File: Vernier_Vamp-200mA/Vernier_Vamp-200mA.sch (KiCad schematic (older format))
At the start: 6 parts, among them J1 Conn_01x02, J2 RJ45, J3 Screw_Terminal_01x04, J5 Conn_Coaxial, J6 Conn_Coaxial, J7 Conn_Coaxial

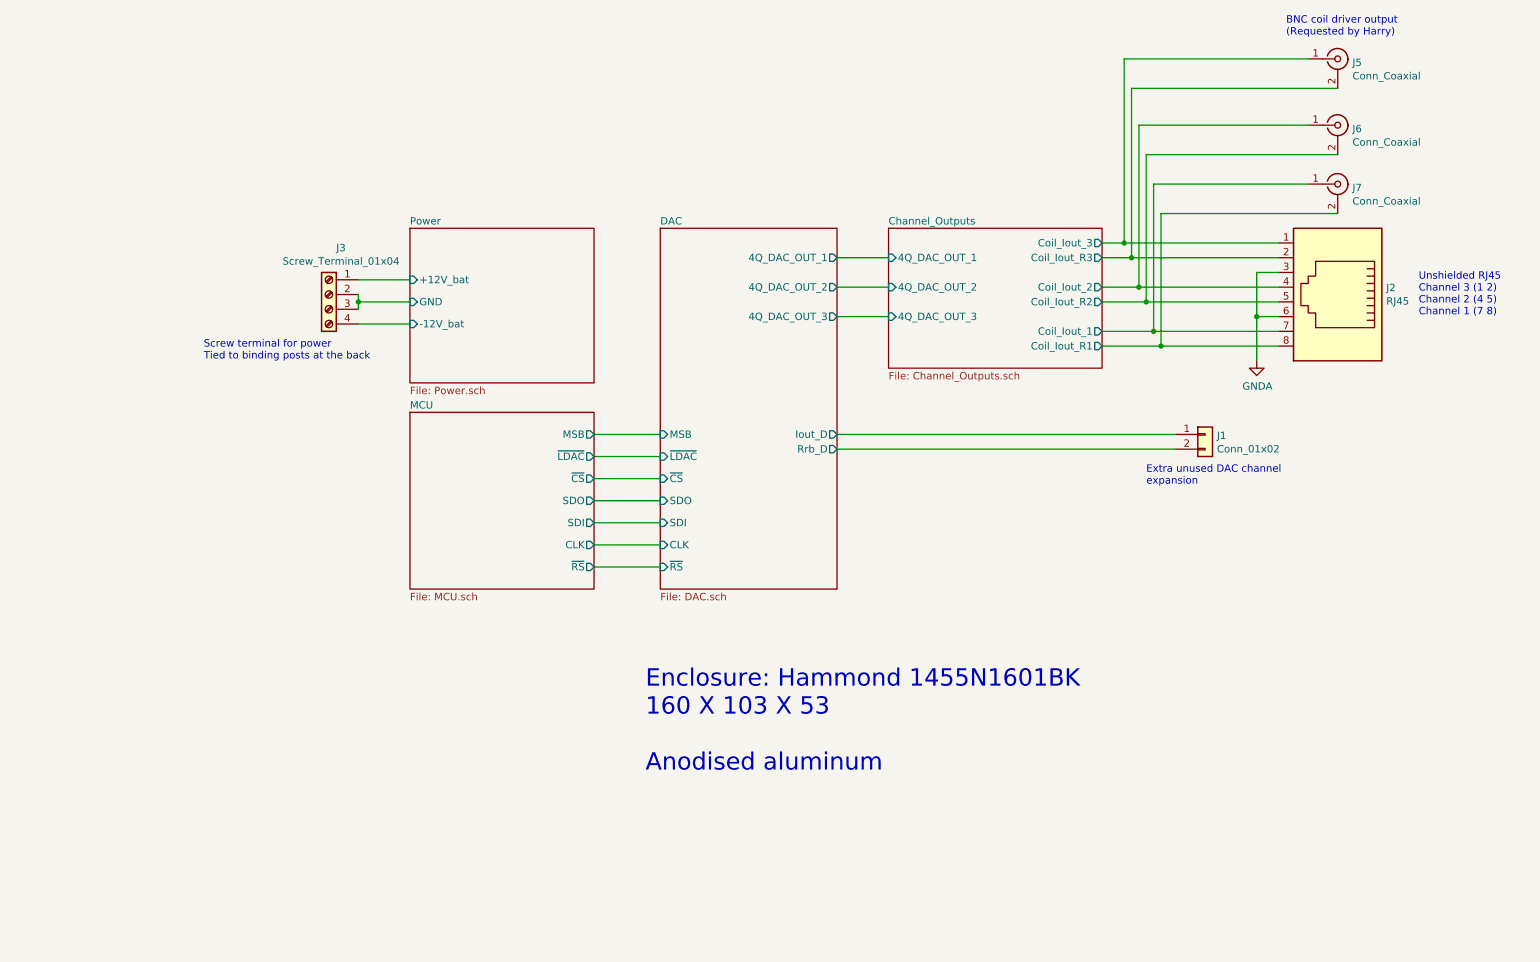
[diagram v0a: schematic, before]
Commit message: Coil driver version 1.0B
Updated coil driver 200mA version with fixes requested by Iain.
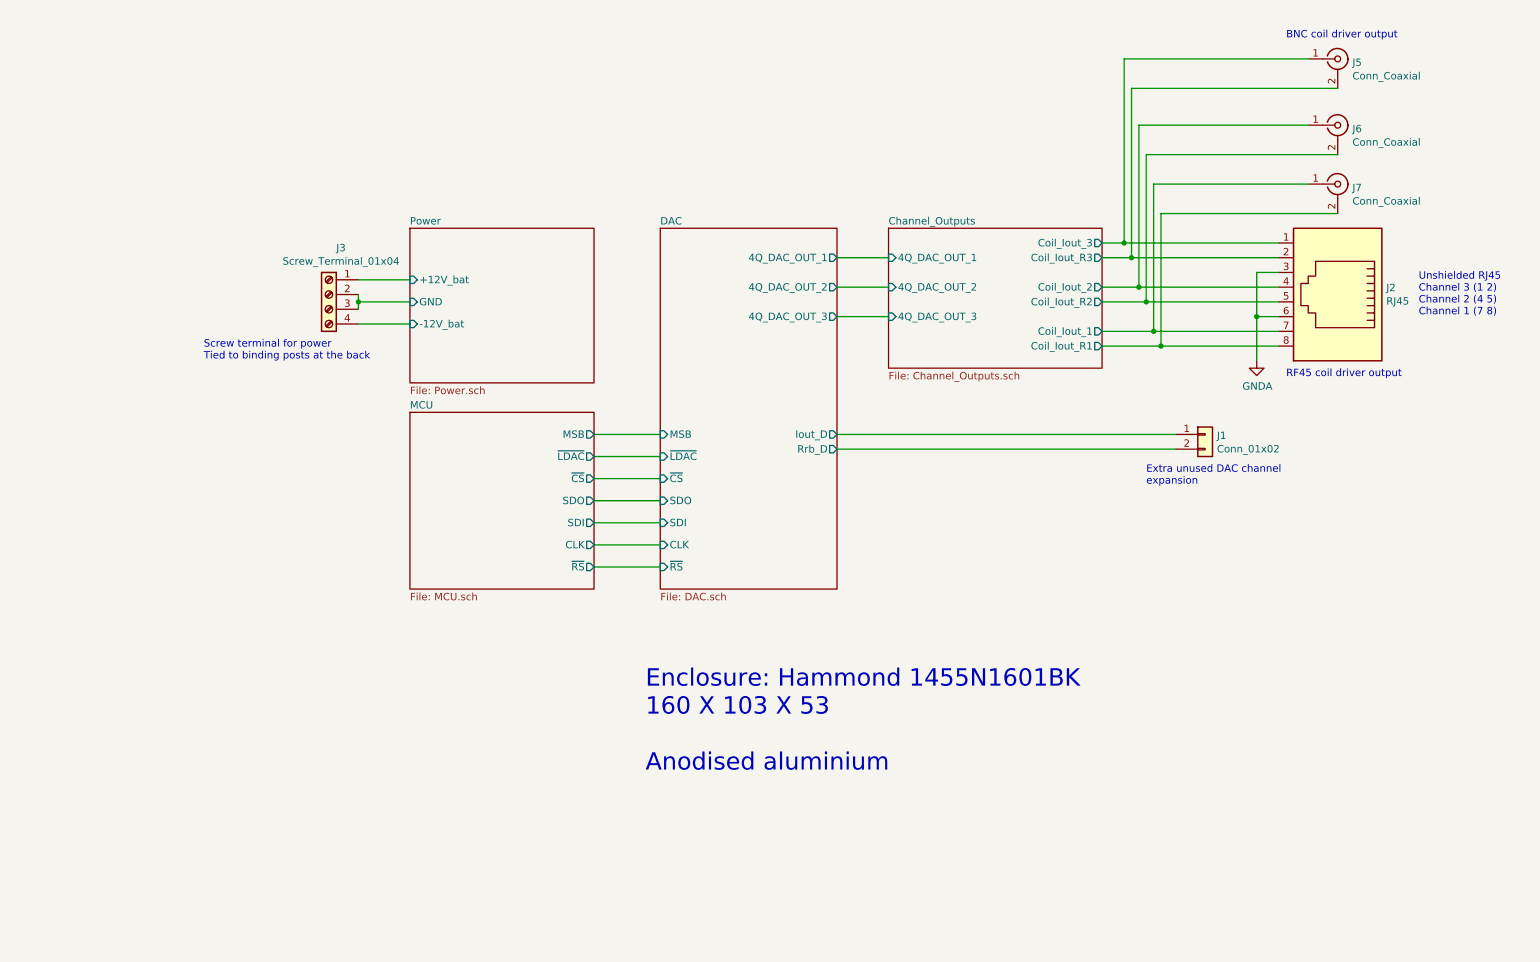
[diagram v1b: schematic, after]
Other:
- note added: "BNC coil driver output\n\n"
- note added: "Enclosure: Hammond 1455N1601BK\n160 X 103 X 53\n\nAnodised aluminium"
- note added: "RF45 coil driver output\n\n"
- note removed: "BNC coil driver output\n(Requested by Harry)"
- note removed: "Enclosure: Hammond 1455N1601BK\n160 X 103 X 53\n\nAnodised aluminum"
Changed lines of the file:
@@
 $Descr A4 11693 8268
 encoding utf-8
-Sheet 1 5
+Sheet 1 7
 Title "\"Vernier Vamp\" Coil Driver - 200mA"
-Date "2020-02-04"
-Rev "1.0A"
+Date "2020-04-27"
+Rev "1.0B"
 Comp "Strathclyde University"
 Comment1 "Designed by: Marcin Mrozowski"
@@
 Wire Wire Line
 	8400 3600 8000 3600
-Text Notes 9250 1500 0    50   ~ 0
-BNC coil driver output\n(Requested by Harry)
+Text Notes 9250 1600 0    50   ~ 0
+BNC coil driver output\n\n
 Text Notes 10150 3400 0    50   ~ 0
 Unshielded RJ45\nChannel 3 (1 2)\nChannel 2 (4 5)\nChannel 1 (7 8)
@@
 Screw terminal for power\nTied to binding posts at the back
 Text Notes 4900 6500 0    118  ~ 0
-Enclosure: Hammond 1455N1601BK\n160 X 103 X 53\n\nAnodised aluminum
+Enclosure: Hammond 1455N1601BK\n160 X 103 X 53\n\nAnodised aluminium
+Text Notes 9250 3900 0    50   ~ 0
+RF45 coil driver output\n\n
 $EndSCHEMATC

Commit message: Schematic and layout changes
Schematic updates:
- Added extra comments
- Added description (BNC channels)
- Moved mounting holes to the title block
- Added an option for connecting low battery indicatior LEDs to either +12V or GND (Comparator pulls to -12V)
- Added a 0R resistor for connecting +12V to Vin of nano
Layout:
- Added board ID and datecode on both sides
- Fixed priority of GND copper islands that were causing issues
- Changed the ground plane to be solid on the connection point (still not ideal but better)
- All components with thermal vias require tented vias so left as default
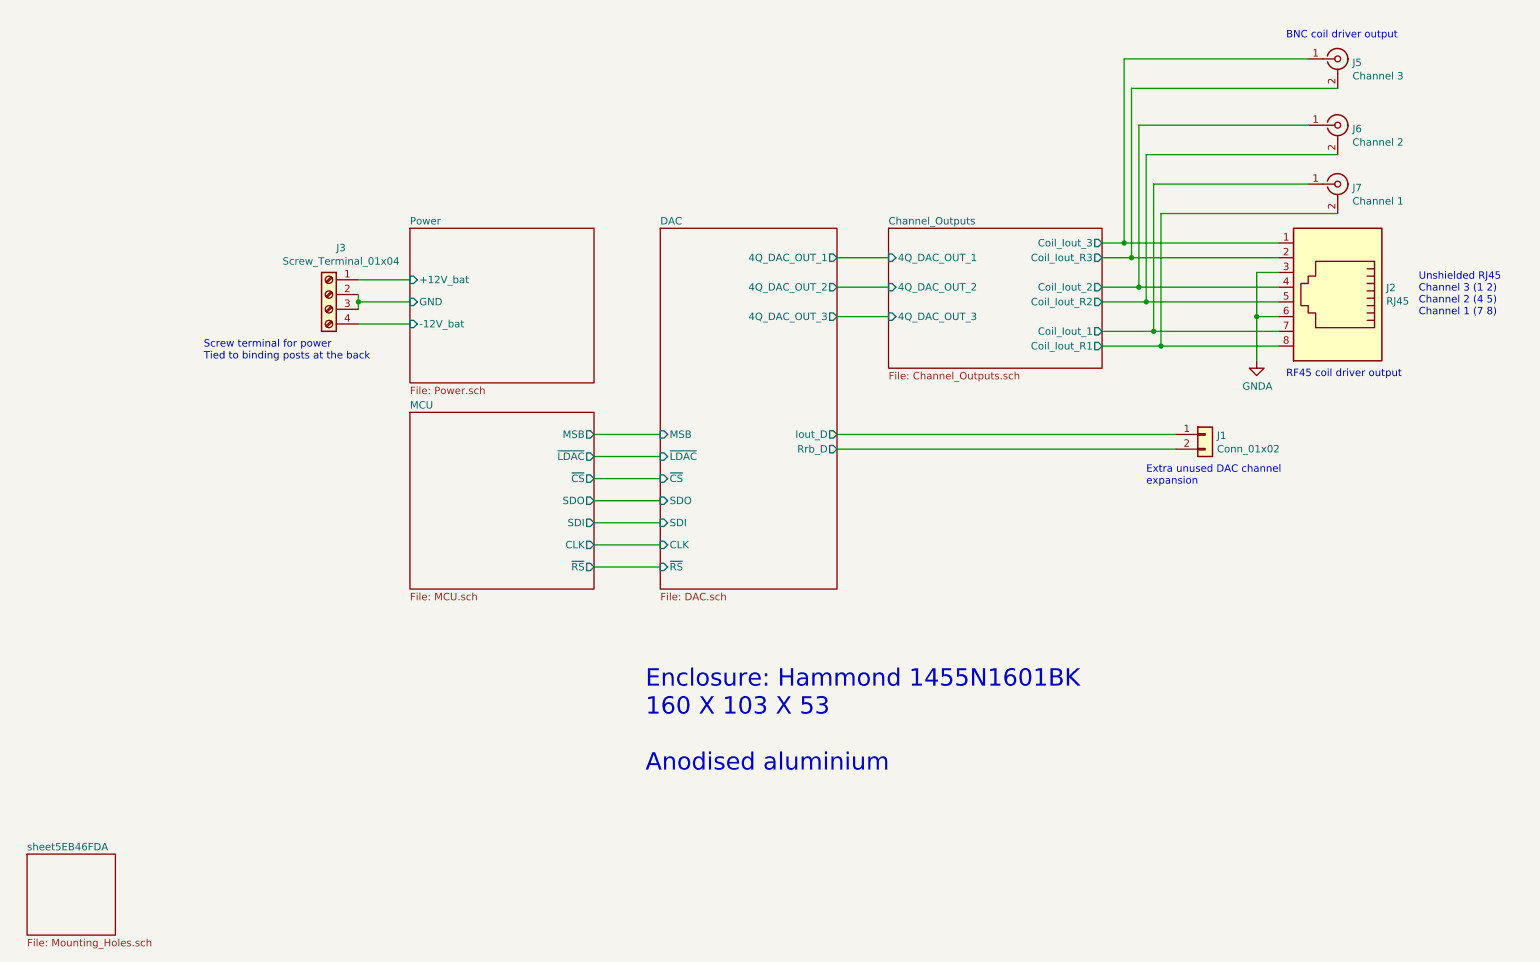
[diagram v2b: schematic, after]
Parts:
- J5: value Conn_Coaxial -> Channel 3
- J6: value Conn_Coaxial -> Channel 2
- J7: value Conn_Coaxial -> Channel 1
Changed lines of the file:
@@
 P 9600 1650
 F 0 "J5" H 9700 1625 50  0000 L CNN
-F 1 "Conn_Coaxial" H 9700 1534 50  0000 L CNN
+F 1 "Channel 3" H 9700 1534 50  0000 L CNN
 F 2 "Connector_Coaxial:BNC_Amphenol_031-6575_Horizontal" H 9600 1650 50  0001 C CNN
 F 3 " ~" H 9600 1650 50  0001 C CNN
@@
 P 9600 2100
 F 0 "J6" H 9700 2075 50  0000 L CNN
-F 1 "Conn_Coaxial" H 9700 1984 50  0000 L CNN
+F 1 "Channel 2" H 9700 1984 50  0000 L CNN
 F 2 "Connector_Coaxial:BNC_Amphenol_031-6575_Horizontal" H 9600 2100 50  0001 C CNN
 F 3 " ~" H 9600 2100 50  0001 C CNN
@@
 P 9600 2500
 F 0 "J7" H 9700 2475 50  0000 L CNN
-F 1 "Conn_Coaxial" H 9700 2384 50  0000 L CNN
+F 1 "Channel 1" H 9700 2384 50  0000 L CNN
 F 2 "Connector_Coaxial:BNC_Amphenol_031-6575_Horizontal" H 9600 2500 50  0001 C CNN
 F 3 " ~" H 9600 2500 50  0001 C CNN
@@
 Text Notes 9250 3900 0    50   ~ 0
 RF45 coil driver output\n\n
+$Sheet
+S 700  7050 600  550
+U 5EB46FDC
+F0 "sheet5EB46FDA" 50
+F1 "Mounting_Holes.sch" 50
+$EndSheet
 $EndSCHEMATC

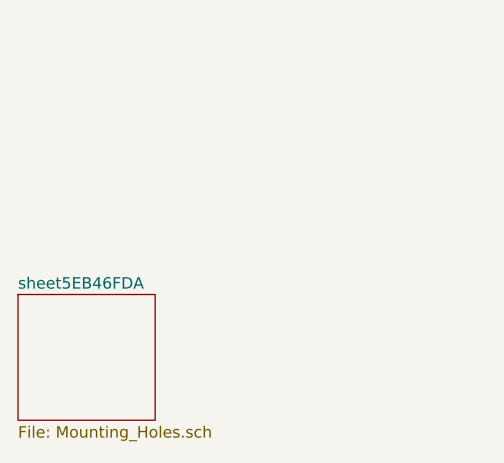
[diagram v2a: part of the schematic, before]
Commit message: 2 mA changes
-2 mA version is now called "low current coil driver" LCCD
- Small changes to the PCB layout
- Shield footprint correction
- General optimisation
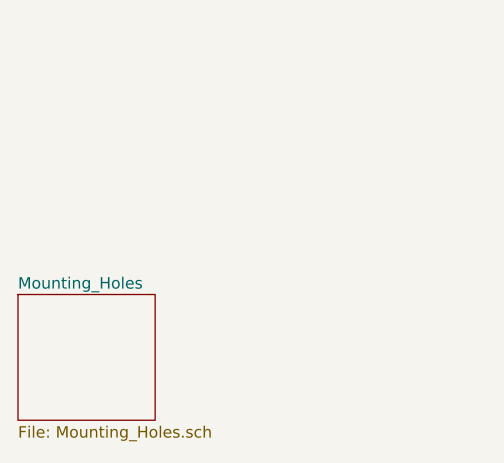
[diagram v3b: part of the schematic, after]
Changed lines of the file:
@@
 S 700  7050 600  550
 U 5EB46FDC
-F0 "sheet5EB46FDA" 50
+F0 "Mounting_Holes" 50
 F1 "Mounting_Holes.sch" 50
 $EndSheet

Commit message: 1.0D Update
LCCD changes
-Addition of trigger for calibration
-PCB optimisation

HCCD changes
-New output stage designed
-Changes from 1.0C applied to HCCD
-New more optimised layout
-New shielding over analog section
-Addition of trigger for calibration

New symbols and footprint creation
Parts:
- added J8: RF_Shield_Two_Pieces, MS570-10F:MS570-10S, symbol Device:RF_Shield_Two_Pieces
- J1: footprint Connector_PinHeader_1.27mm:PinHeader_1x02_P1.27mm_Vertical -> Dummy_conn_01x02:PinSocket_1x02_P1.00mm_Vertical_CUSTOM_CYD
- J5, J6, J7: footprint Connector_Coaxial:BNC_Amphenol_031-6575_Horizontal -> Connector_Coaxial:BNC_Amphenol_B6252HB-NPP3G-50_Horizontal
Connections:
- net GNDA: now also J8.1 (Shield)
